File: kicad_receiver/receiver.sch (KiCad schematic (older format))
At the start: 59 parts, among them J1 Conn_01x05_Male, J2 M1+, J3 M1-, J4 M2+, J5 M2-, J6 CHG+5V, J7 CHG-, J8 BAT+, J9 BAT-, Q1 MMBT3904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

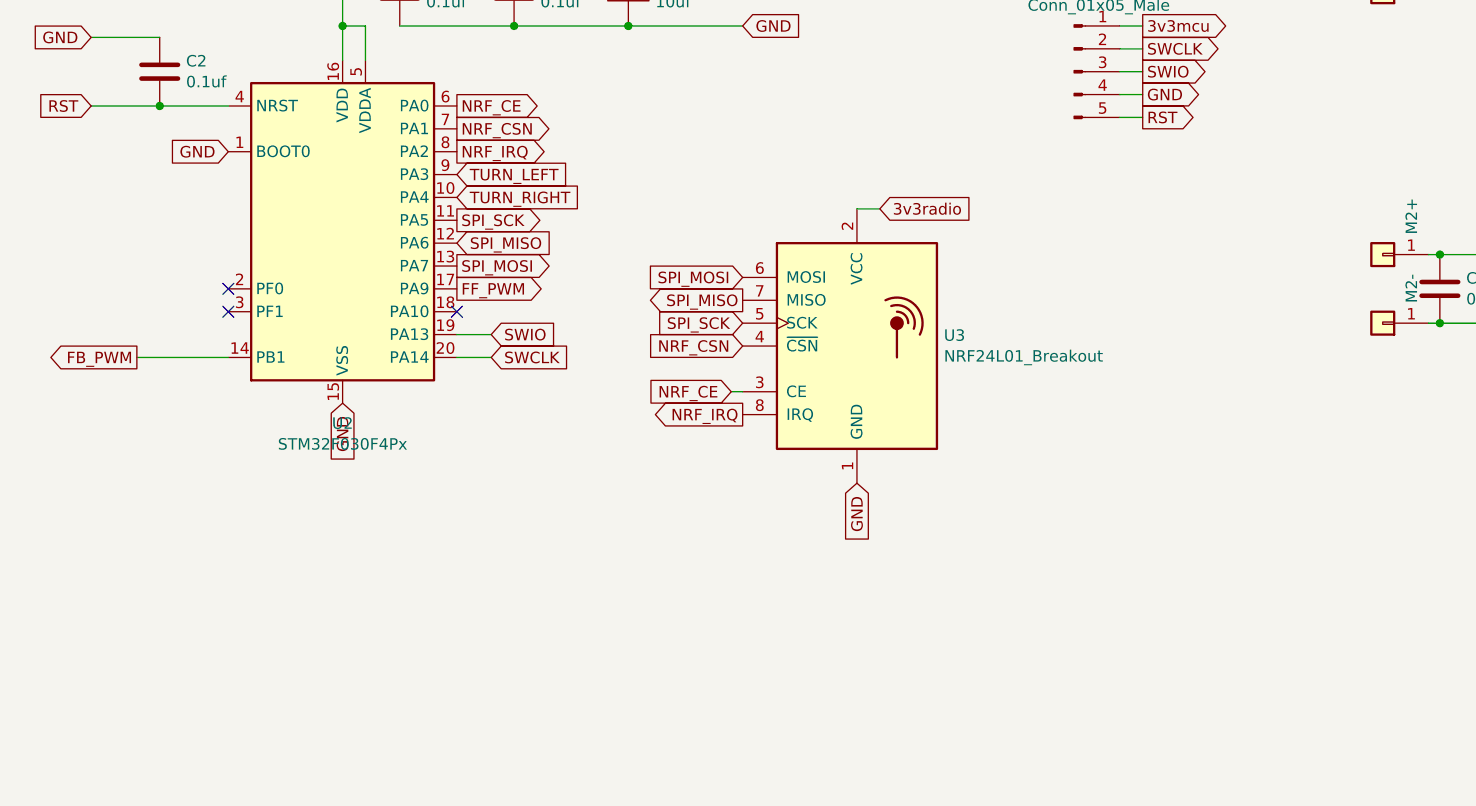
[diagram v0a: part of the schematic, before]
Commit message: new route done
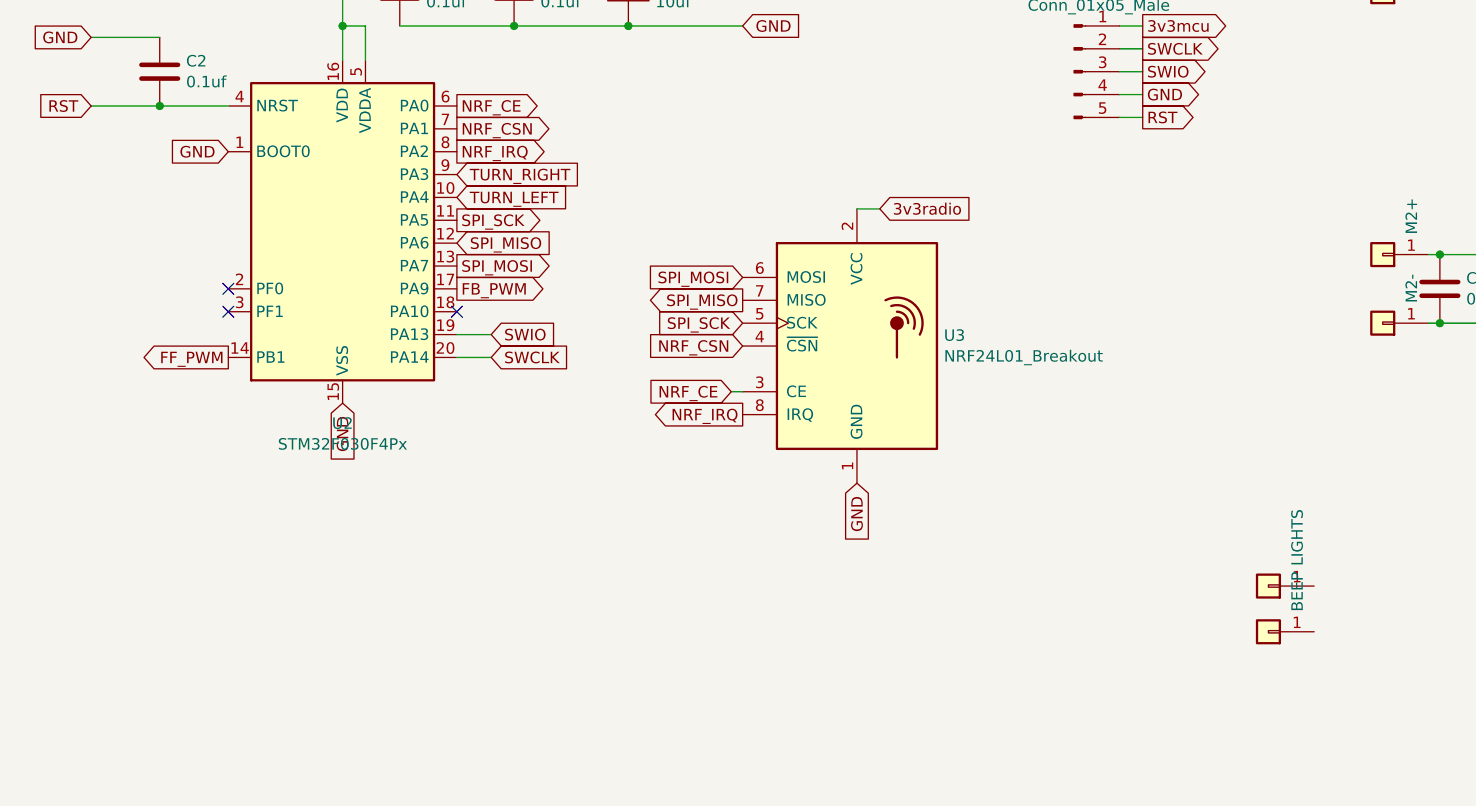
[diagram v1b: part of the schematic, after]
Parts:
- added J10: LIGHTS, TestPoint:TestPoint_THTPad_4.0x4.0mm_Drill2.0mm, symbol Connector_Generic:Conn_01x01
- added J11: BEEP, TestPoint:TestPoint_THTPad_4.0x4.0mm_Drill2.0mm, symbol Connector_Generic:Conn_01x01
- J2, J3, J4, J5, J6, J7, J8, J9: footprint TestPoint:TestPoint_Pad_2.5x2.5mm -> TestPoint:TestPoint_THTPad_4.0x4.0mm_Drill2.0mm
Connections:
- wire segments 192 -> 191
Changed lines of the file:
@@
 F 0 "J6" V 7164 4762 50  0001 R CNN
 F 1 "CHG+5V" V 7073 4762 50  0000 R CNN
-F 2 "TestPoint:TestPoint_Pad_2.5x2.5mm" H 7200 4850 50  0001 C CNN
+F 2 "TestPoint:TestPoint_THTPad_4.0x4.0mm_Drill2.0mm" H 7200 4850 50  0001 C CNN
 F 3 "~" H 7200 4850 50  0001 C CNN
 	1    7200 4850
 	-1   0    0    1
 $EndComp
+Text GLabel 1500 3550 0    50   Output ~ 0
+FF_PWM
 Text GLabel 2500 3250 2    50   Output ~ 0
-FF_PWM
-Text GLabel 1100 3550 0    50   Output ~ 0
 FB_PWM
-Wire Wire Line
-	1500 3550 1100 3550
 $Comp
 L Device:R R5
@@
 Text GLabel 3800 1400 0    50   Input ~ 0
 GND
+Text GLabel 2500 2850 2    50   Input ~ 0
+TURN_LEFT
 Text GLabel 2500 2750 2    50   Input ~ 0
-TURN_LEFT
-Text GLabel 2500 2850 2    50   Input ~ 0
 TURN_RIGHT
 $Comp
@@
 F 0 "J2" V 6514 1562 50  0001 R CNN
 F 1 "M1+" V 6423 1562 50  0000 R CNN
-F 2 "TestPoint:TestPoint_Pad_2.5x2.5mm" H 6550 1650 50  0001 C CNN
+F 2 "TestPoint:TestPoint_THTPad_4.0x4.0mm_Drill2.0mm" H 6550 1650 50  0001 C CNN
 F 3 "~" H 6550 1650 50  0001 C CNN
 	1    6550 1650
@@
 F 0 "J3" V 6514 1862 50  0001 R CNN
 F 1 "M1-" V 6423 1862 50  0000 R CNN
-F 2 "TestPoint:TestPoint_Pad_2.5x2.5mm" H 6550 1950 50  0001 C CNN
+F 2 "TestPoint:TestPoint_THTPad_4.0x4.0mm_Drill2.0mm" H 6550 1950 50  0001 C CNN
 F 3 "~" H 6550 1950 50  0001 C CNN
 	1    6550 1950
@@
 F 0 "J4" V 6514 3012 50  0001 R CNN
 F 1 "M2+" V 6423 3012 50  0000 R CNN
-F 2 "TestPoint:TestPoint_Pad_2.5x2.5mm" H 6550 3100 50  0001 C CNN
+F 2 "TestPoint:TestPoint_THTPad_4.0x4.0mm_Drill2.0mm" H 6550 3100 50  0001 C CNN
 F 3 "~" H 6550 3100 50  0001 C CNN
 	1    6550 3100
@@
 F 0 "J5" V 6514 3312 50  0001 R CNN
 F 1 "M2-" V 6423 3312 50  0000 R CNN
-F 2 "TestPoint:TestPoint_Pad_2.5x2.5mm" H 6550 3400 50  0001 C CNN
+F 2 "TestPoint:TestPoint_THTPad_4.0x4.0mm_Drill2.0mm" H 6550 3400 50  0001 C CNN
 F 3 "~" H 6550 3400 50  0001 C CNN
 	1    6550 3400
@@
 F 0 "J7" V 7164 5812 50  0001 R CNN
 F 1 "CHG-" V 7073 5812 50  0000 R CNN
-F 2 "TestPoint:TestPoint_Pad_2.5x2.5mm" H 7200 5900 50  0001 C CNN
+F 2 "TestPoint:TestPoint_THTPad_4.0x4.0mm_Drill2.0mm" H 7200 5900 50  0001 C CNN
 F 3 "~" H 7200 5900 50  0001 C CNN
 	1    7200 5900
@@
 F 0 "J8" V 10364 4862 50  0001 R CNN
 F 1 "BAT+" V 10273 4862 50  0000 R CNN
-F 2 "TestPoint:TestPoint_Pad_2.5x2.5mm" H 10400 4950 50  0001 C CNN
+F 2 "TestPoint:TestPoint_THTPad_4.0x4.0mm_Drill2.0mm" H 10400 4950 50  0001 C CNN
 F 3 "~" H 10400 4950 50  0001 C CNN
 	1    10400 4950
@@
 F 0 "J9" V 10364 5812 50  0001 R CNN
 F 1 "BAT-" V 10273 5812 50  0000 R CNN
-F 2 "TestPoint:TestPoint_Pad_2.5x2.5mm" H 10400 5900 50  0001 C CNN
+F 2 "TestPoint:TestPoint_THTPad_4.0x4.0mm_Drill2.0mm" H 10400 5900 50  0001 C CNN
 F 3 "~" H 10400 5900 50  0001 C CNN
 	1    10400 5900
@@
 Wire Wire Line
 	9300 2650 9300 2400
+$Comp
+L Connector_Generic:Conn_01x01 J10
+U 1 1 5DF09767
+P 6050 4550
+F 0 "J10" V 6014 4462 50  0001 R CNN
+F 1 "LIGHTS" V 5923 4462 50  0000 R CNN
+F 2 "TestPoint:TestPoint_THTPad_4.0x4.0mm_Drill2.0mm" H 6050 4550 50  0001 C CNN
+F 3 "~" H 6050 4550 50  0001 C CNN
+	1    6050 4550
+	-1   0    0    1
+$EndComp
+$Comp
+L Connector_Generic:Conn_01x01 J11
+U 1 1 5DF09F8C
+P 6050 4750
+F 0 "J11" V 6014 4662 50  0001 R CNN
+F 1 "BEEP" V 5923 4662 50  0000 R CNN
+F 2 "TestPoint:TestPoint_THTPad_4.0x4.0mm_Drill2.0mm" H 6050 4750 50  0001 C CNN
+F 3 "~" H 6050 4750 50  0001 C CNN
+	1    6050 4750
+	-1   0    0    1
+$EndComp
 $EndSCHEMATC

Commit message: mosfets added, piezo scheme added
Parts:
- removed Q1, Q2, Q3, Q4: MMBT3904, Package_TO_SOT_SMD:SOT-23, symbol Transistor_BJT:MMBT3904
- removed R22, R23: 100, Resistor_SMD:R_0603_1608Metric_Pad1.05x0.95mm_HandSolder, symbol Device:R
- added C17, C18: 10uf, Capacitor_SMD:CP_Elec_4x3, symbol Device:CP
- added Q1, Q2, Q3, Q4: BSS138, Package_TO_SOT_SMD:SOT-23, symbol Transistor_FET:BSS138
- added R10: 1-10, Resistor_SMD:R_0603_1608Metric_Pad1.05x0.95mm_HandSolder, symbol Device:R
- added R11, R12: 2k2, Resistor_SMD:R_0603_1608Metric_Pad1.05x0.95mm_HandSolder, symbol Device:R
- added R13: 100k, Resistor_SMD:R_0603_1608Metric_Pad1.05x0.95mm_HandSolder, symbol Device:R
- added U8: LM358, Package_SO:SOIC-8_3.9x4.9mm_P1.27mm, symbol lm358:LM358
- added Y1: Crystal, TestPoint:TestPoint_2Pads_Pitch5.08mm_Drill1.3mm, symbol Device:Crystal
- R15: value 100 -> 100k
- R17: value 100 -> 1k
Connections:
- net labels added: VIBRO_SIGNAL
- wire segments 191 -> 215

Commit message: piezo route done
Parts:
- removed C18: 10uf, Capacitor_SMD:CP_Elec_4x3, symbol Device:CP
- removed J10: LIGHTS, TestPoint:TestPoint_THTPad_4.0x4.0mm_Drill2.0mm, symbol Connector_Generic:Conn_01x01
- removed J11: BEEP, TestPoint:TestPoint_THTPad_4.0x4.0mm_Drill2.0mm, symbol Connector_Generic:Conn_01x01
- C17: footprint Capacitor_SMD:CP_Elec_4x3 -> Capacitor_SMD:C_0805_2012Metric_Pad1.15x1.40mm_HandSolder; symbol Device:CP -> Device:C
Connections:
- net NRF_IRQ: now also U2.18 (PA10); no longer U2.8 (PA2)
- net VIBRO_SIGNAL: now also U2.8 (PA2)
- no-connect marks 3 -> 2
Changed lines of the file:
@@
 Wire Wire Line
 	3700 3700 3750 3700
-NoConn ~ 2500 3350
 Wire Wire Line
 	4000 1400 4700 1400
@@
 Text GLabel 3750 3800 0    50   Output ~ 0
 NRF_IRQ
-Text GLabel 2500 2650 2    50   Output ~ 0
+Text GLabel 2500 3350 2    50   Output ~ 0
 NRF_IRQ
 Text GLabel 2500 2450 2    50   Output ~ 0
@@
 Wire Wire Line
 	10450 900  10950 900
-$Comp
-L Connector_Generic:Conn_01x01 J10
-U 1 1 5DF09767
-P 6050 4550
-F 0 "J10" V 6014 4462 50  0001 R CNN
-F 1 "LIGHTS" V 5923 4462 50  0000 R CNN
-F 2 "TestPoint:TestPoint_THTPad_4.0x4.0mm_Drill2.0mm" H 6050 4550 50  0001 C CNN
-F 3 "~" H 6050 4550 50  0001 C CNN
-	1    6050 4550
-	-1   0    0    1
-$EndComp
-$Comp
-L Connector_Generic:Conn_01x01 J11
-U 1 1 5DF09F8C
-P 6050 4750
-F 0 "J11" V 6014 4662 50  0001 R CNN
-F 1 "BEEP" V 5923 4662 50  0000 R CNN
-F 2 "TestPoint:TestPoint_THTPad_4.0x4.0mm_Drill2.0mm" H 6050 4750 50  0001 C CNN
-F 3 "~" H 6050 4750 50  0001 C CNN
-	1    6050 4750
-	-1   0    0    1
-$EndComp
 Wire Wire Line
 	9650 2400 10100 2400
@@
 $EndComp
 $Comp
-L Device:CP C18
-U 1 1 5DA8BDFA
-P 4200 6050
-F 0 "C18" H 4318 6096 50  0000 L CNN
-F 1 "10uf" H 4318 6005 50  0000 L CNN
-F 2 "Capacitor_SMD:CP_Elec_4x3" H 4238 5900 50  0001 C CNN
-F 3 "~" H 4200 6050 50  0001 C CNN
-	1    4200 6050
-	1    0    0    -1
-$EndComp
-$Comp
-L Device:CP C17
+L Device:C C17
 U 1 1 5DA97984
 P 2100 6300
 F 0 "C17" H 2218 6346 50  0000 L CNN
 F 1 "10uf" H 2218 6255 50  0000 L CNN
-F 2 "Capacitor_SMD:CP_Elec_4x3" H 2138 6150 50  0001 C CNN
+F 2 "Capacitor_SMD:C_0805_2012Metric_Pad1.15x1.40mm_HandSolder" H 2138 6150 50  0001 C CNN
 F 3 "~" H 2100 6300 50  0001 C CNN
 	1    2100 6300
@@
 Connection ~ 3100 6450
 Wire Wire Line
-	3100 6450 4200 6450
-Wire Wire Line
-	3100 5000 4200 5000
-Wire Wire Line
-	4200 5900 4200 5000
-Connection ~ 4200 5000
-Wire Wire Line
-	4200 5000 4350 5000
-Wire Wire Line
-	4200 6200 4200 6450
-Wire Wire Line
-	4200 6450 4400 6450
-Connection ~ 4200 6450
-Wire Wire Line
 	4000 5750 4300 5750
 Wire Wire Line
@@
 Wire Wire Line
 	2100 5300 2400 5300
+Wire Wire Line
+	3100 5000 4350 5000
+Wire Wire Line
+	3100 6450 4400 6450
+Text GLabel 2500 2650 2    50   Input ~ 0
+VIBRO_SIGNAL
 $EndSCHEMATC

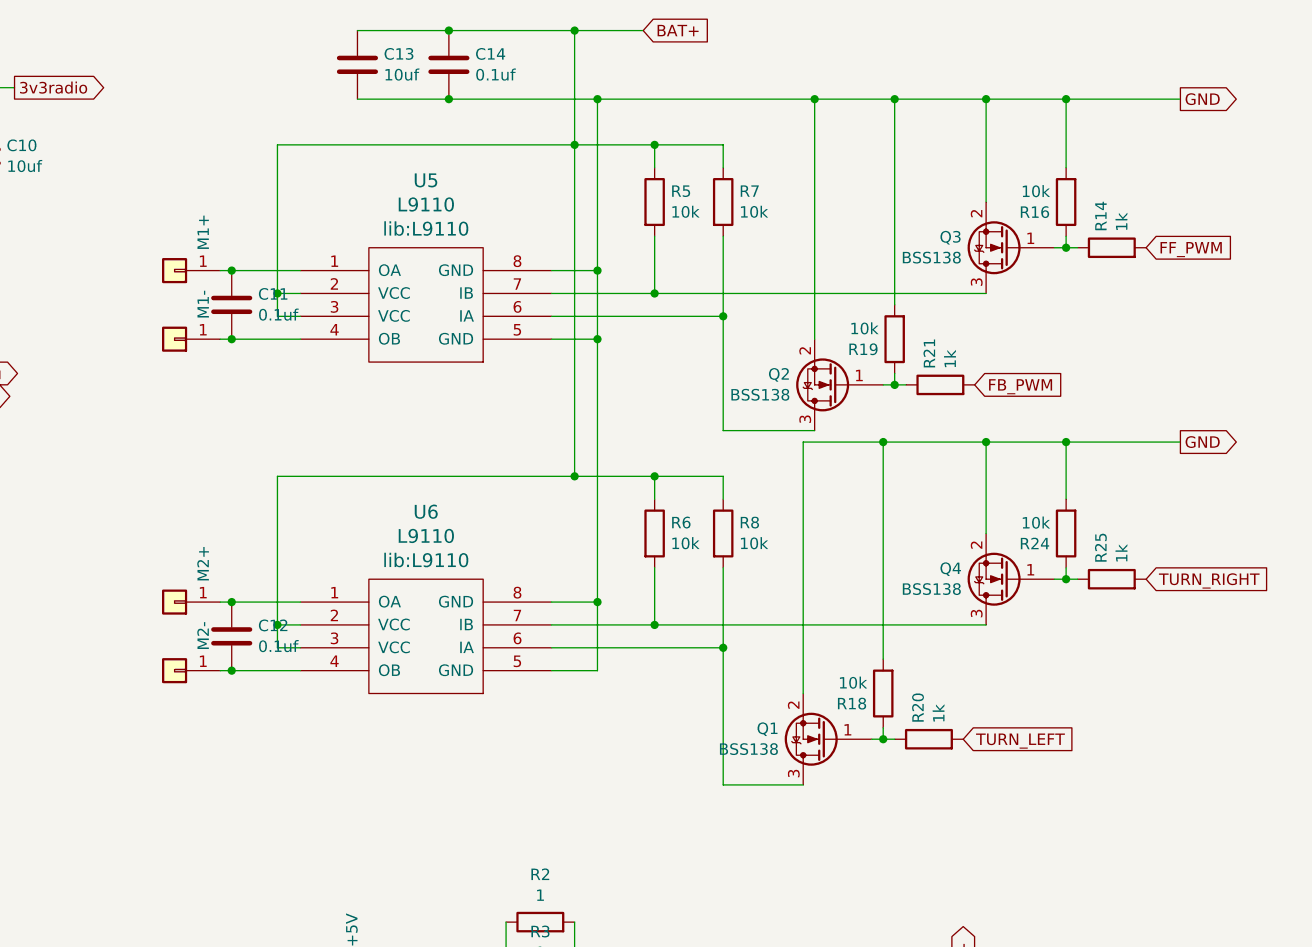
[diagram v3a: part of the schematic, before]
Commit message: mosfets removed, now use pure pwm signals
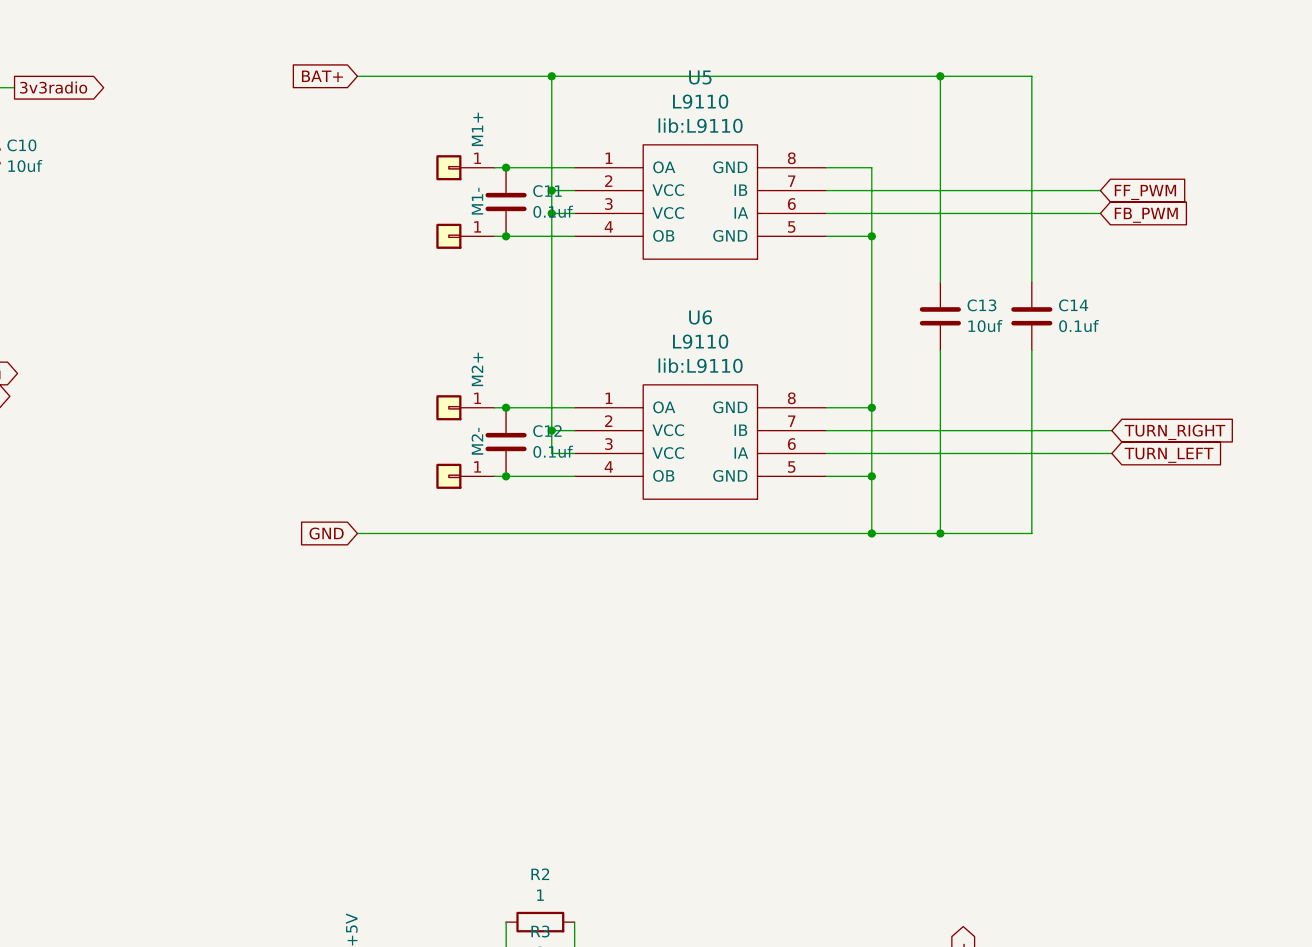
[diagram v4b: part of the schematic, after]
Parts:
- removed Q1, Q2, Q3, Q4: BSS138, Package_TO_SOT_SMD:SOT-23, symbol Transistor_FET:BSS138
- removed R14, R20, R21, R25: 1k, Resistor_SMD:R_0603_1608Metric_Pad1.05x0.95mm_HandSolder, symbol Device:R
- removed R16, R18, R19, R24, R5, R6, R7, R8: 10k, Resistor_SMD:R_0603_1608Metric_Pad1.05x0.95mm_HandSolder, symbol Device:R
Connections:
- net FB_PWM: now also U5.6 (IA)
- net FF_PWM: now also U5.7 (IB)
- net TURN_LEFT: now also U6.6 (IA)
- net TURN_RIGHT: now also U6.7 (IB)
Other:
- moved on the sheet: C11, C12, C13, C14, U5, U6
